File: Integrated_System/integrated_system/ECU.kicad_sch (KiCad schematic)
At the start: 36 parts, among them J1 Jack-DC, J2 Fan 1, J3 Fan 2, J4 Fan 3, Q2 TN0702N3, Q3 TN0702N3, Q4 TN0702N3, U1 DC to DC Buck Converter 12V t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, U2 BME680, U5 SGP30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

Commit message: Fixed LED placement
LED Placement and added switch
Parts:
- removed R7, R8, R9: 5.1k, symbol Device:R_Small_US
- added D10: GREEN_LED, symbol Device:LED
- added D11: RED_LED, symbol Device:LED
- added ON/OFF_SWITCH: SW_DPDT_x2, symbol Switch:SW_DPDT_x2
- added R13, R14: 5.1k, symbol Device:R_Small_US
- D4, D5: value LED -> GREEN_LED
- D6: value LED -> YELLOW_LED
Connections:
- net +12V: now also ON/OFF_SWITCH.2 (B); no longer C1.1, C2.1, D1.1 (K), D2.1 (K), D3.1 (K), J2.2 (Pin_2), J3.2 (Pin_2), J4.2 (Pin_2), U1.1 (Vin+)
- net GND: now also D4.1 (K), D5.1 (K), D6.1 (K), R13.1, R14.1; no longer D4.2 (A), D5.2 (A), D6.2 (A), Q2.3 (S), Q3.3 (S), Q4.3 (S)
- new net: D10.1 (K), R14.2
- new net: D5.2 (A), Q4.3 (S)
- new net: D6.2 (A), Q2.3 (S)
- new net: D11.1 (K), R13.2
- new net: D11.2 (A), ON/OFF_SWITCH.3 (C)
- new net: D4.2 (A), Q3.3 (S)
- new net FP_12V: C1.1, C2.1, D1.1 (K), D10.2 (A), D2.1 (K), D3.1 (K), J2.2 (Pin_2), J3.2 (Pin_2), J4.2 (Pin_2), ON/OFF_SWITCH.1 (A), U1.1 (Vin+)
- no-connect marks 8 -> 9
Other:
- moved on the sheet: C1, C2, D5, U1

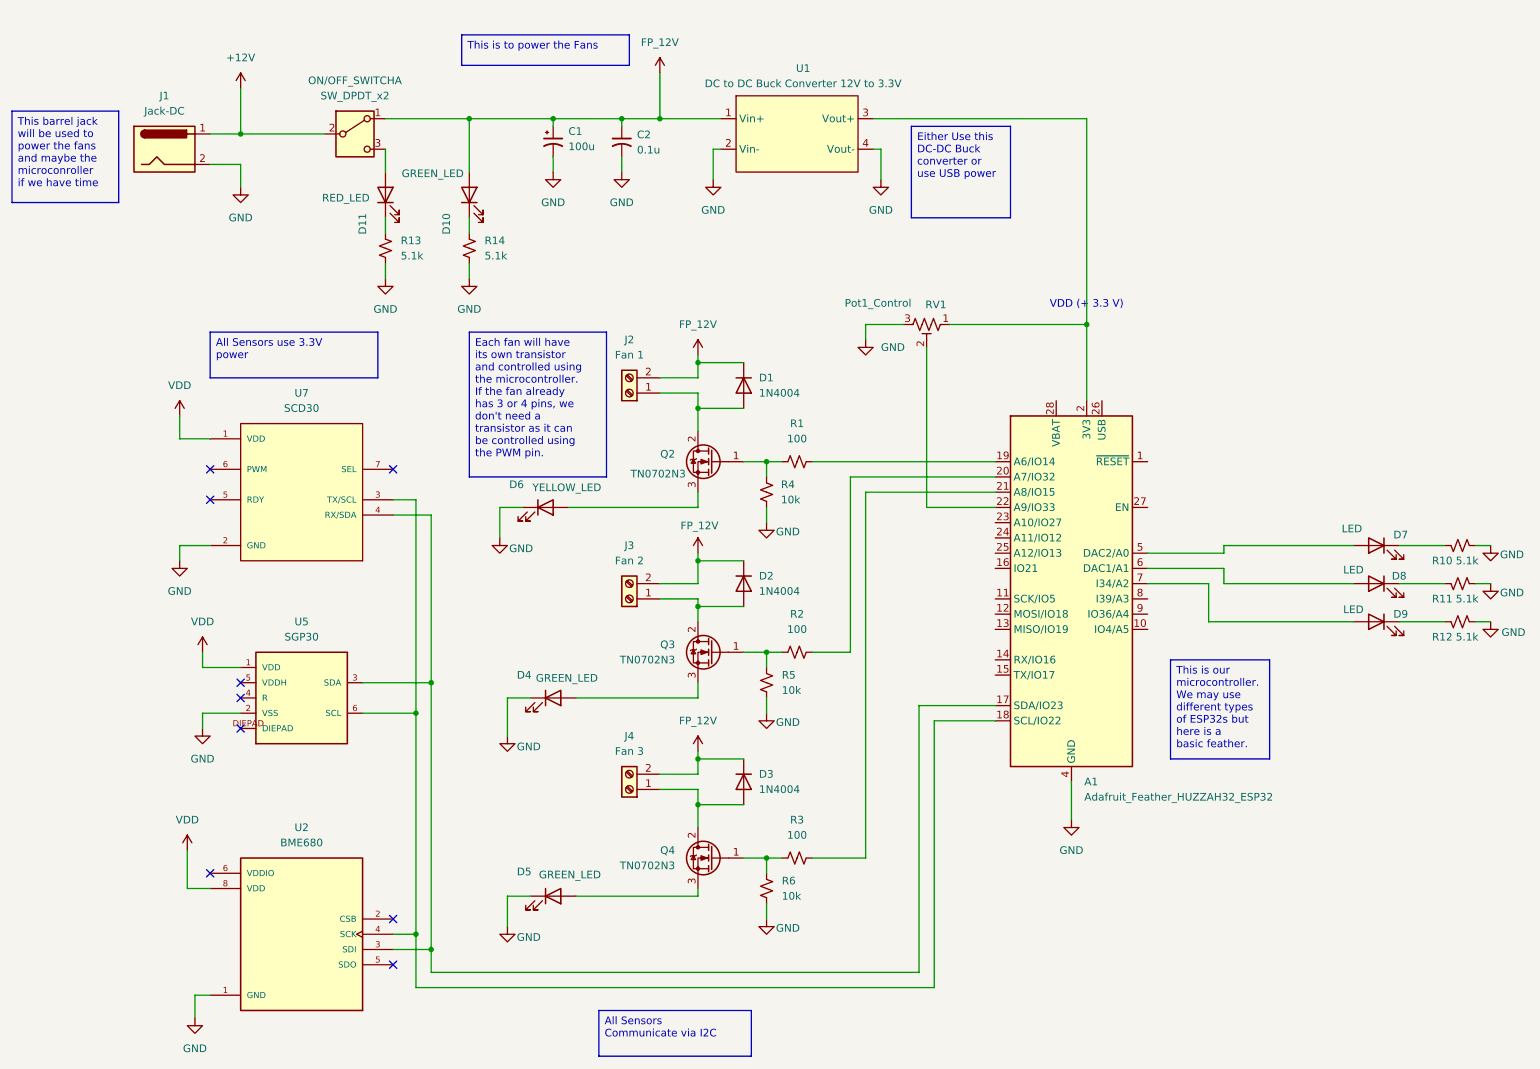
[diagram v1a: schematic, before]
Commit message: Switched to the right pins
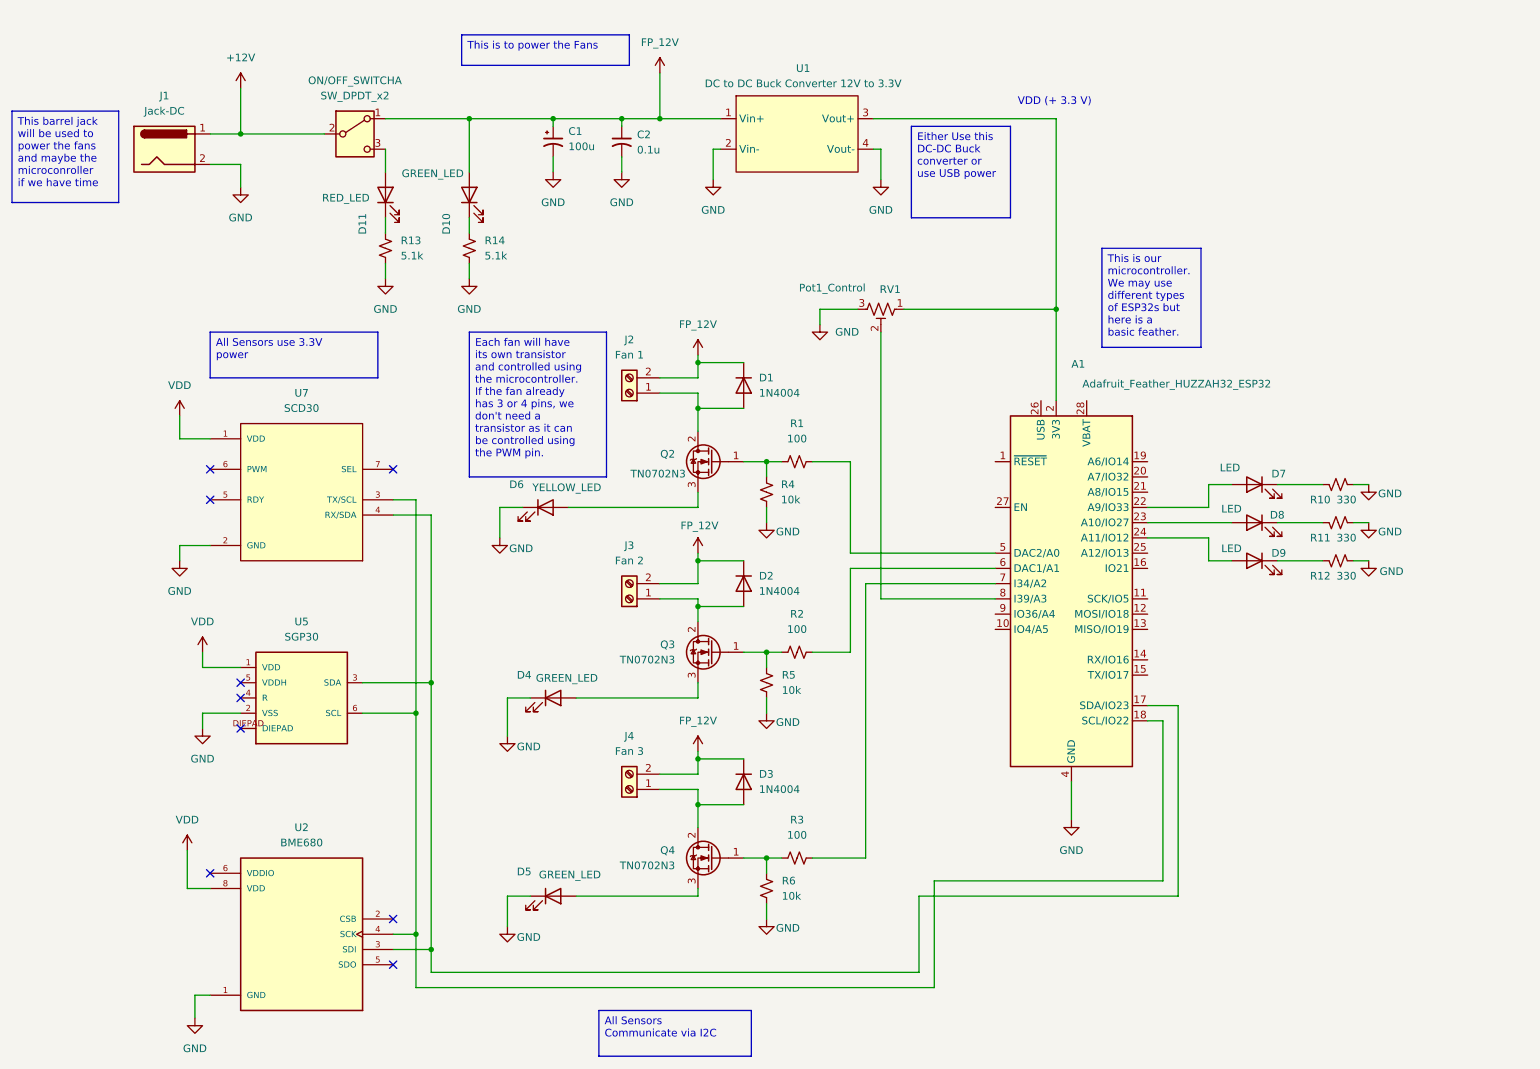
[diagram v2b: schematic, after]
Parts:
- R10, R11, R12: value 5.1k -> 330
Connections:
- net at R1.2: now also A1.5 (DAC2/A0); no longer A1.19 (A6/IO14)
- net at D9.2 (A): now also A1.24 (A11/IO12); no longer A1.7 (I34/A2)
- net at D8.2 (A): now also A1.23 (A10/IO27); no longer A1.6 (DAC1/A1)
- net at A1.20 (A7/IO32): no longer R2.2
- net at A1.21 (A8/IO15): no longer R3.2
- net at A1.22 (A9/IO33): now also D7.2 (A); no longer RV1.2
- net at A1.8 (I39/A3): now also RV1.2
- new net: A1.6 (DAC1/A1), R2.2
- new net: A1.7 (I34/A2), R3.2
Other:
- moved on the sheet: D7, D8, D9, R10, R11, R12, RV1
